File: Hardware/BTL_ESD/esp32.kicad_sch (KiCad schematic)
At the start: 11 parts, among them SW3 ENABLE, SW4 FLASH, U5 ESP32-WROOM-32E__4MB_HIGH_TEM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

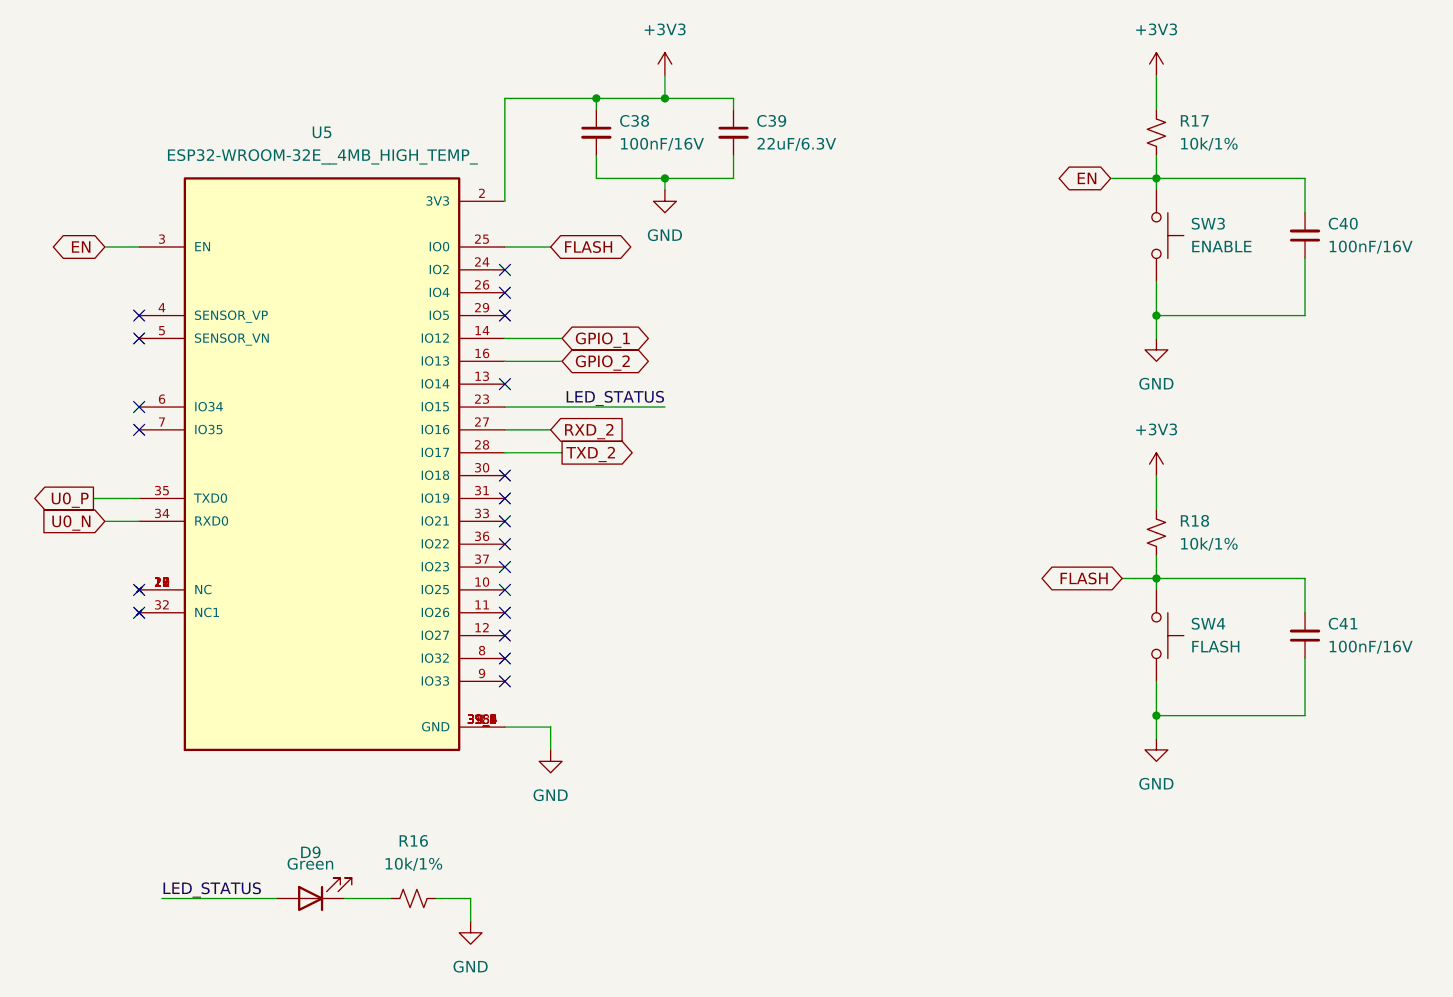
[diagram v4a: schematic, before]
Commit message: file:STM32: update structure folder
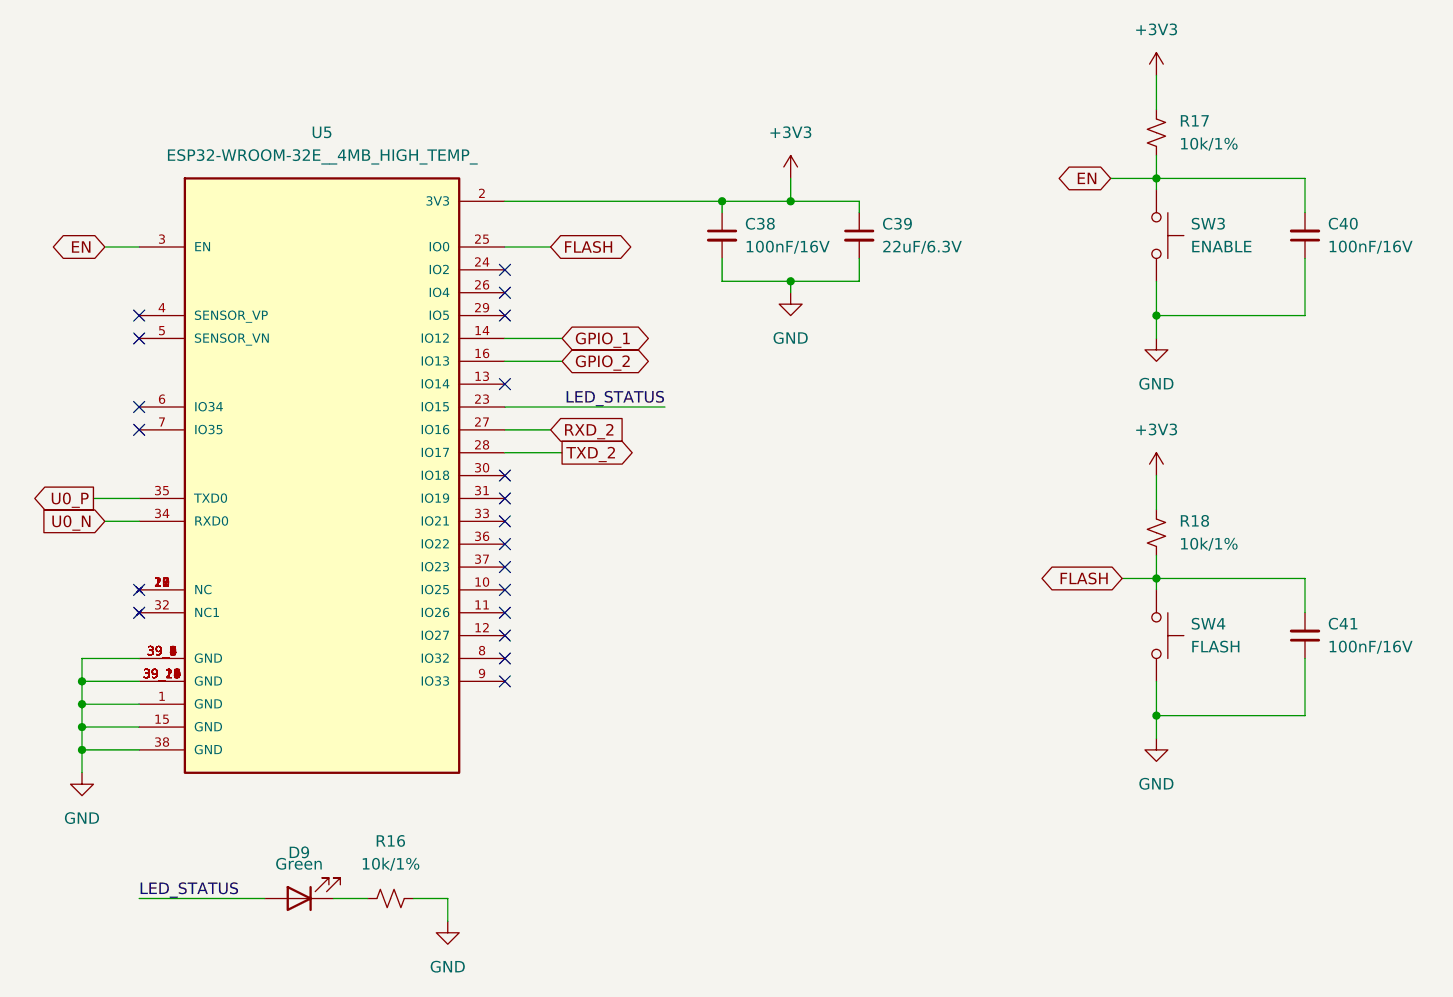
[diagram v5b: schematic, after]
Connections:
- net GND: now also U5.39_10 (GND), U5.39_11 (GND), U5.39_12 (GND), U5.39_13 (GND), U5.39_14 (GND), U5.39_15 (GND), U5.39_16 (GND), U5.39_17 (GND), U5.39_18 (GND), U5.39_19 (GND), U5.39_20 (GND), U5.39_21 (GND)
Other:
- moved on the sheet: C38, C39, D9, R16

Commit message: code:ESP32: update uart driver, main.c && hardware file pcb
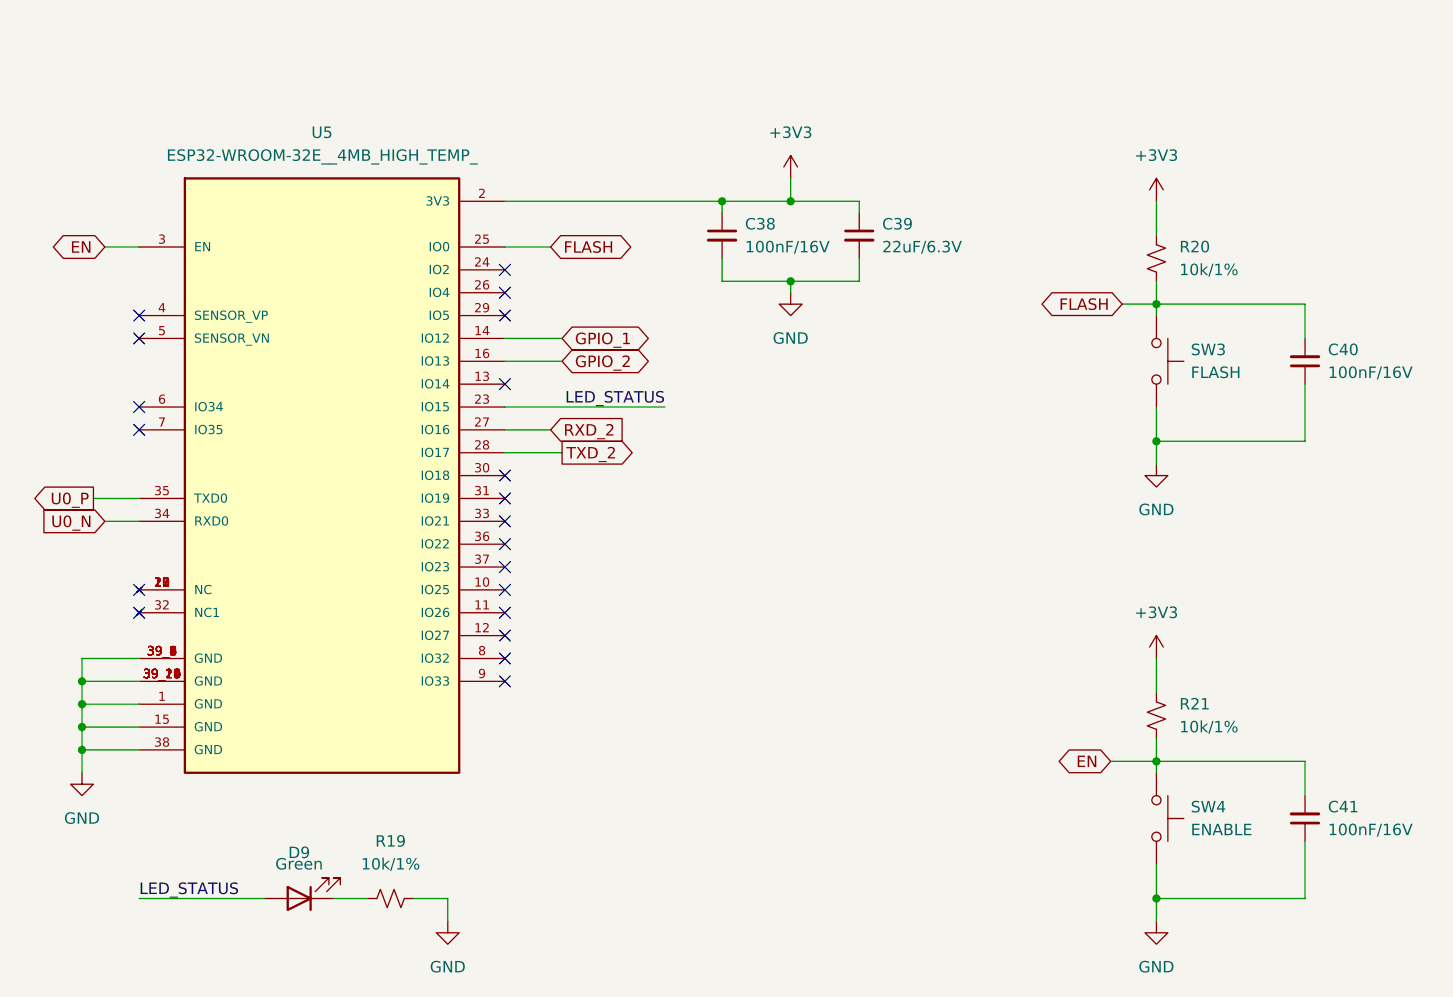
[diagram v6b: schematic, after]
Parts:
- renumbered C41 to C40, C40 to C41, R16 to R19, R18 to R20, R17 to R21, SW4 to SW3, SW3 to SW4
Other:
- moved on the sheet: C40, C41, R20, R21, SW3, SW4
